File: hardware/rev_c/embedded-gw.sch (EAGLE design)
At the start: 56 parts, among them J1 DM3BT-DSF-PEJS, J2 TC2030-JLINK-NL, J3 USB-A-MALE-PLUG, Q1 QS5K2TR, U1 AP7362A-33SP-13, U2 BT840X, U3 CP2102N-20, U4 ESDR0502N, U5 ESP32-WROVER-E, U6 ESP32-WROVER-E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

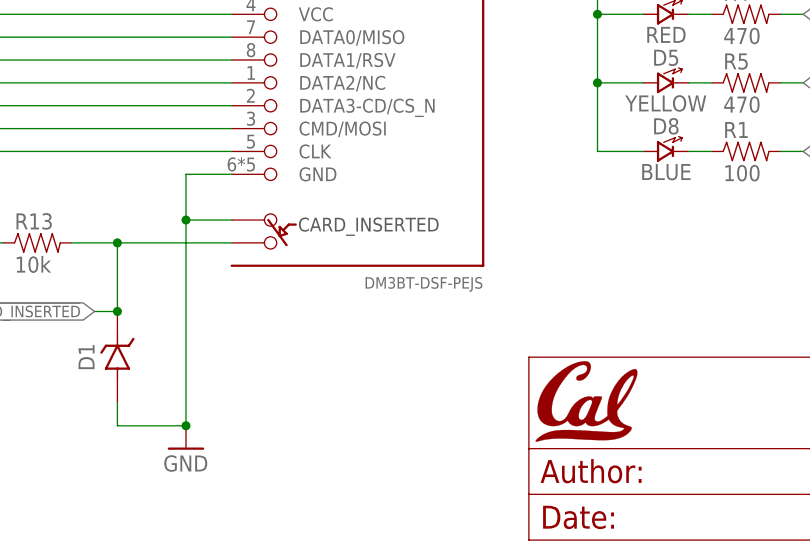
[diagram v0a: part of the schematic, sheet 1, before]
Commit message: replace sd card slot
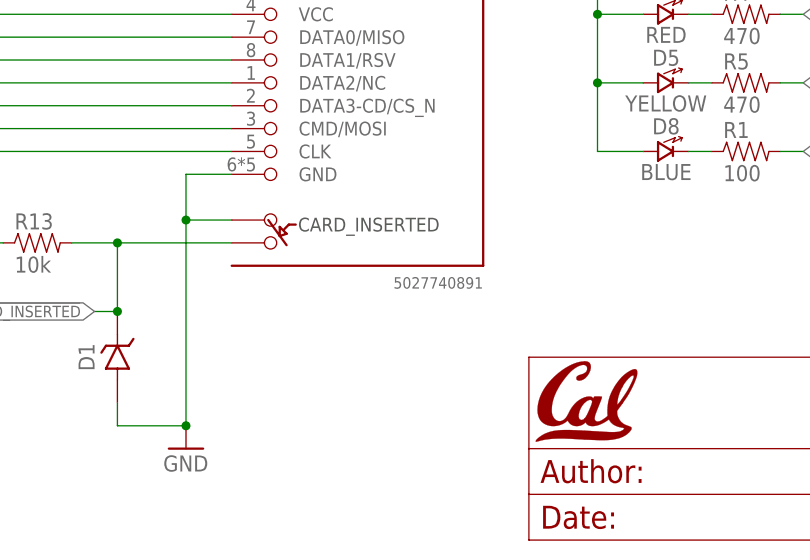
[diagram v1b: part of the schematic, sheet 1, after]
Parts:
- J1: value DM3BT-DSF-PEJS -> 5027740891; device connector:DM3BT-DSF-PEJS -> connector:5027740891

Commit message: change sclk to pin 16 instead of PA 19
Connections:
- net NRF_SCLK: now also U2.P0.16; no longer U2.P0.19
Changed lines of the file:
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@@
 <net name="NRF_SCLK" class="0">
 <segment>
-<pinref part="U2" gate="G$1" pin="P0.19"/>
-<wire x1="106.68" y1="83.82" x2="104.14" y2="83.82" width="0.1524" layer="91"/>
-<label x="104.14" y="83.82" size="1.27" layer="95" rot="R180" xref="yes"/>
+<pinref part="U2" gate="G$1" pin="P0.16"/>
+<wire x1="106.68" y1="91.44" x2="104.14" y2="91.44" width="0.1524" layer="91"/>
+<label x="104.14" y="91.44" size="1.27" layer="95" rot="R180" xref="yes"/>
 </segment>
 </net>

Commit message: update BOM
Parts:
- R19: DIGIKEY 13-RT0402FRE0722K1LCT-ND -> 13-RT0402FRE0747K5LCT-ND; MPN RT0402FRE0722K1L -> RT0402FRE0747K5L
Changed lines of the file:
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@@
 </part>
 <part name="R19" library="passives" library_urn="urn:adsk.eagle:library:29018993" deviceset="RESISTOR" device="0402_RES" package3d_urn="urn:adsk.eagle:package:29019086/1" value="47.5k">
-<attribute name="DIGIKEY" value="13-RT0402FRE0722K1LCT-ND"/>
-<attribute name="MPN" value="RT0402FRE0722K1L"/>
+<attribute name="DIGIKEY" value="13-RT0402FRE0747K5LCT-ND"/>
+<attribute name="MPN" value="RT0402FRE0747K5L"/>
 </part>
 <part name="R18" library="passives" library_urn="urn:adsk.eagle:library:29018993" deviceset="RESISTOR" device="0402_RES" package3d_urn="urn:adsk.eagle:package:29019086/1" value="22.1k">
